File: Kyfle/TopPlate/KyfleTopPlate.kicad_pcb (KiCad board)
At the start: 2 copper layers, 164 x 146.3 mm, 44 parts, among them SW2 KEY_SWITCH, SW2 PRO MICRO

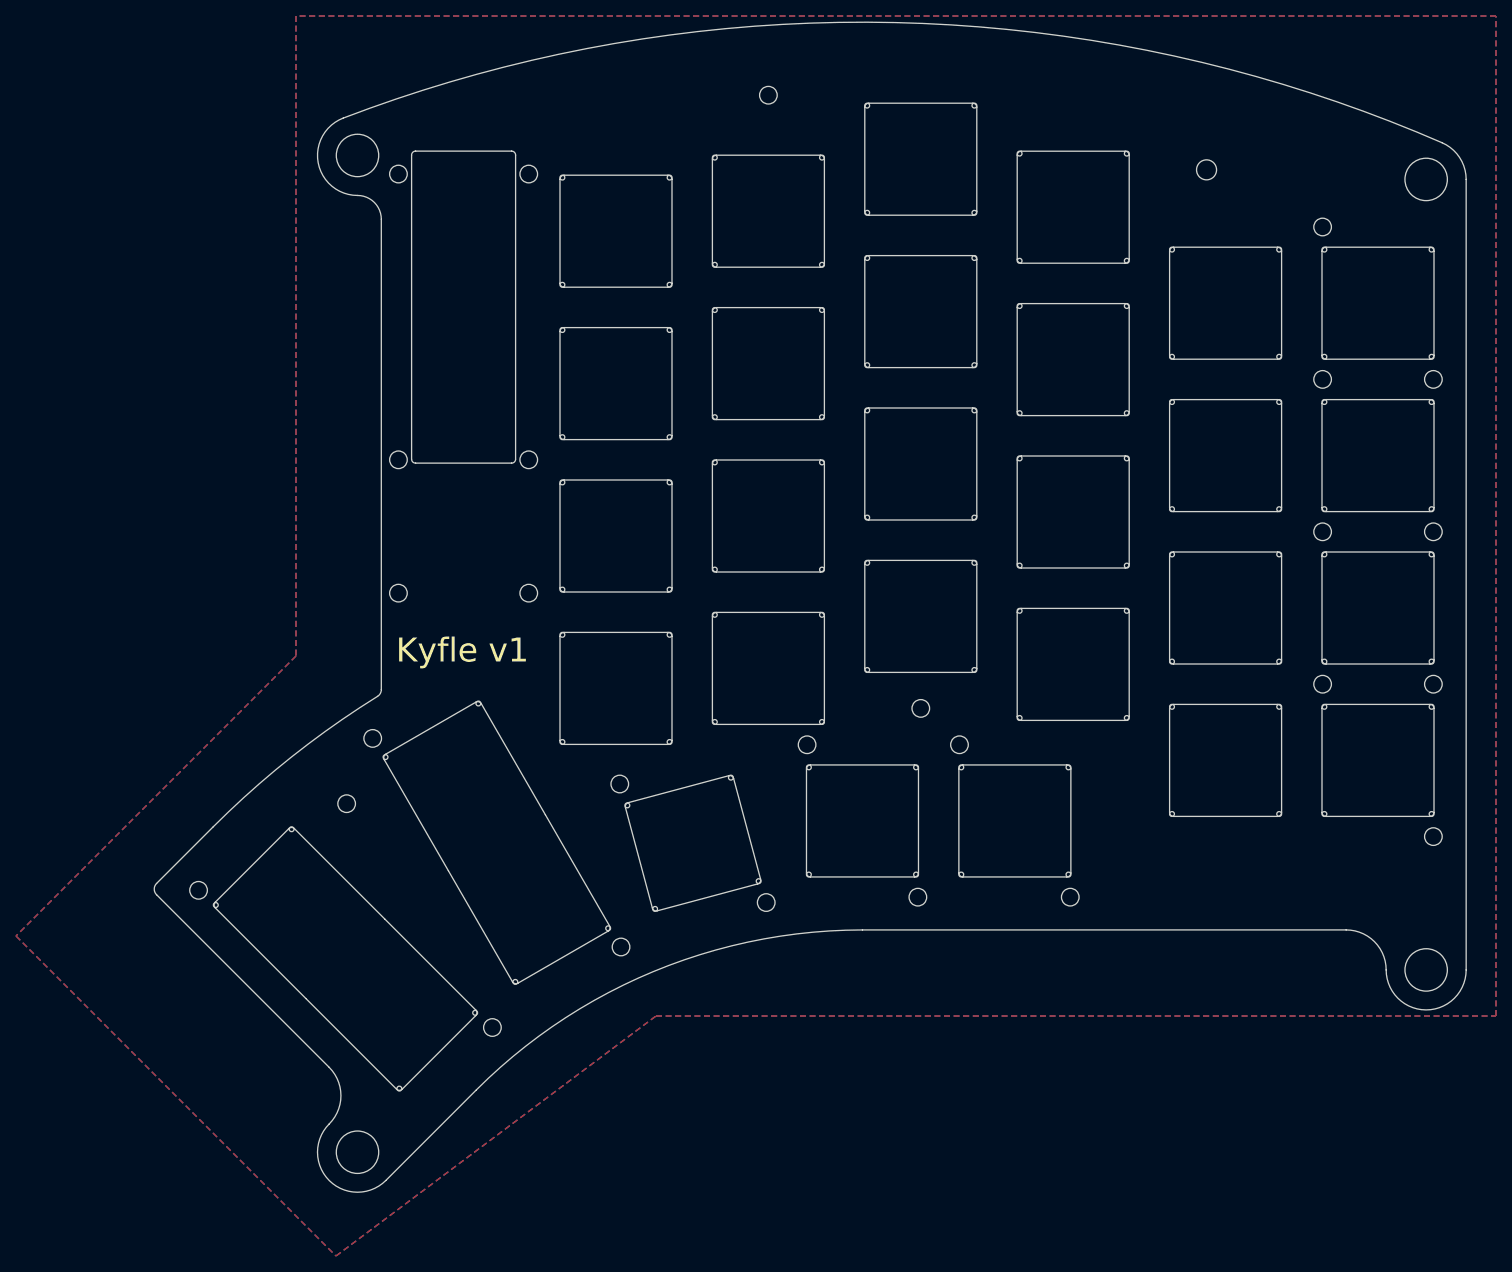
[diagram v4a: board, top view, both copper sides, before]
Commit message: Resized M2 slots and holes to 2mm instead of 2.2mm
After receiving M2 hardware, I noticed 2mm opening would provide a tighter and less wobbly fit than the typical M2 clearance of 2.2mm.

Also, finished the silkscreen of bottom plate, as well as M2 holes for encoders in top plate.
At this point, both top and bottom plate could be considered finished.
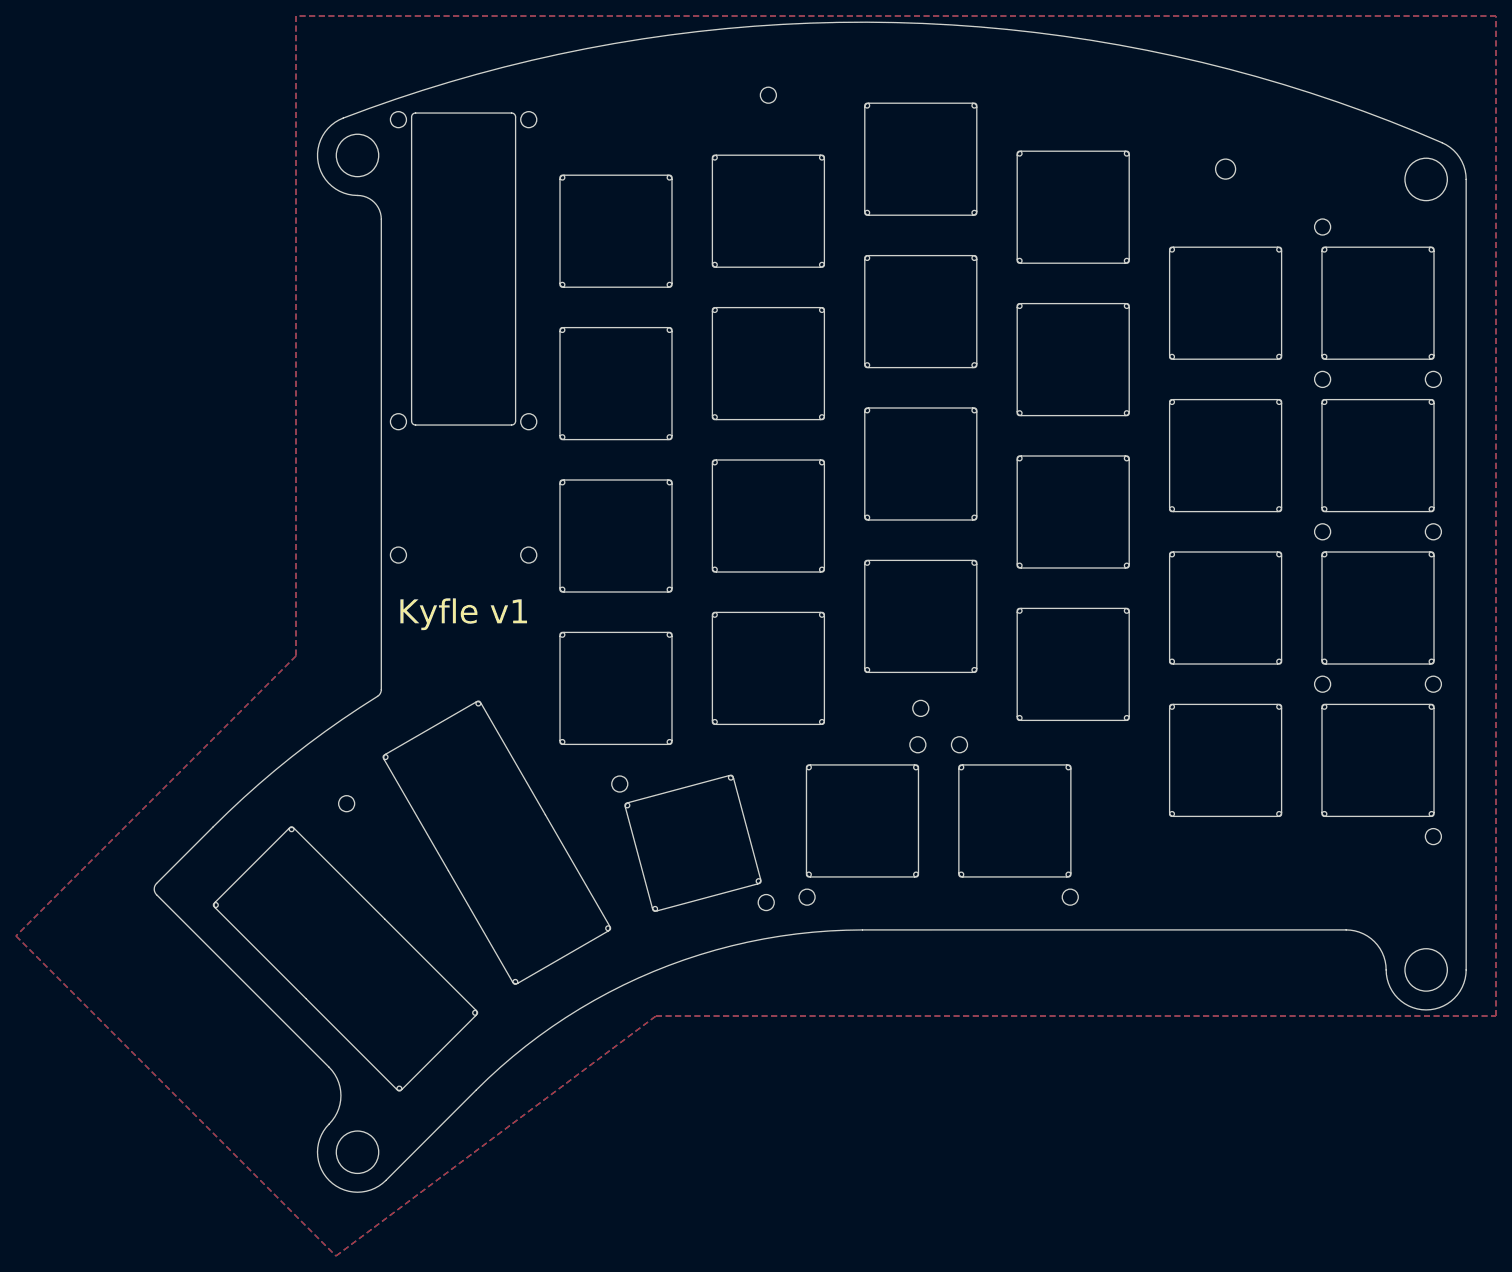
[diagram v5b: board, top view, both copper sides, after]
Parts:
- removed the REF** at (103.8, 37.3)
- removed the REF** at (120.0, 89.6)
- removed the REF** at (103.8, 89.6)
- removed the REF** at (103.8, 73.0)
- removed the REF** at (120.0, 73.0)
- removed the REF** at (120.0, 37.3)
- SW2: moved to B.Cu
- moved SW2 4.76 mm to (111.9, 58.7)
- moved SW2 2.38 mm to (207.2, 36.6)
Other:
- rule pad_to_mask_clearance: 0.2 -> 0

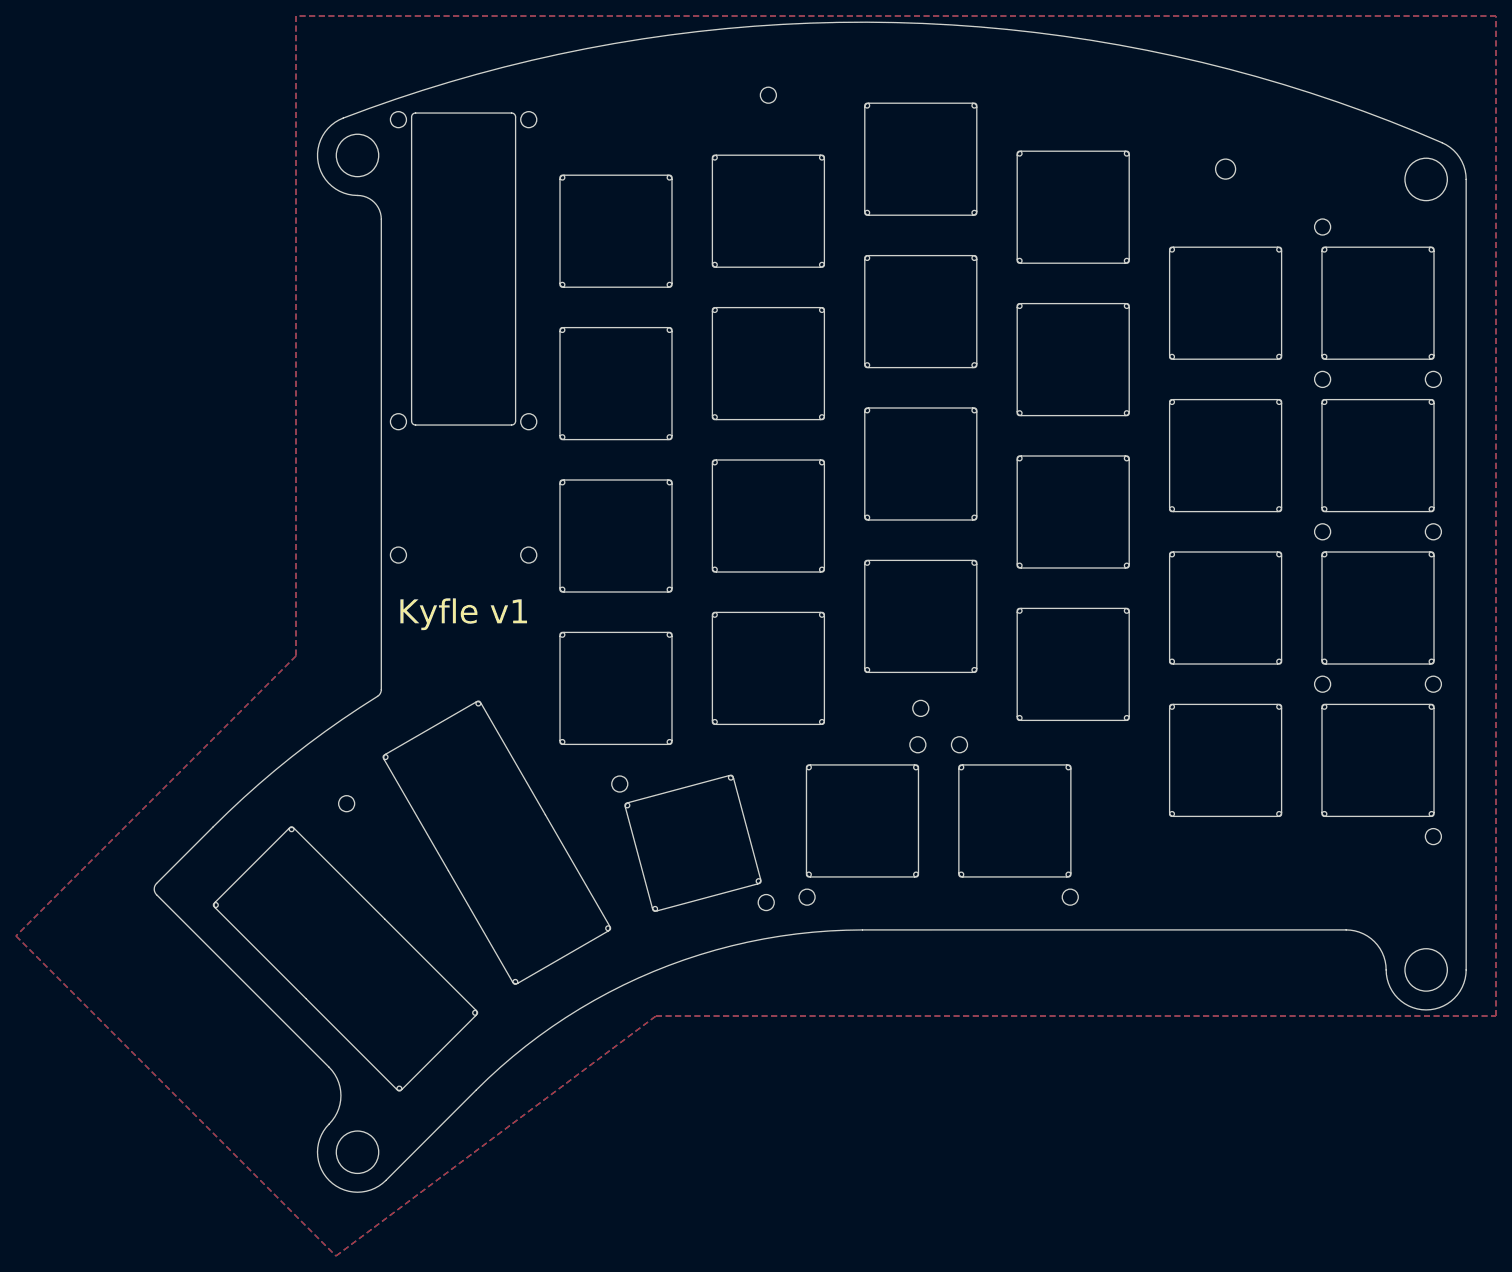
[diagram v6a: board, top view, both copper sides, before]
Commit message: It is never done. Adding plethora of plate variants.
- Variant of the default top plate with less routing involved
- Variant of a top plate allowing to slide the switches around
- Variant of that last top plate with less routing involved

Also moving few minor things here and there.
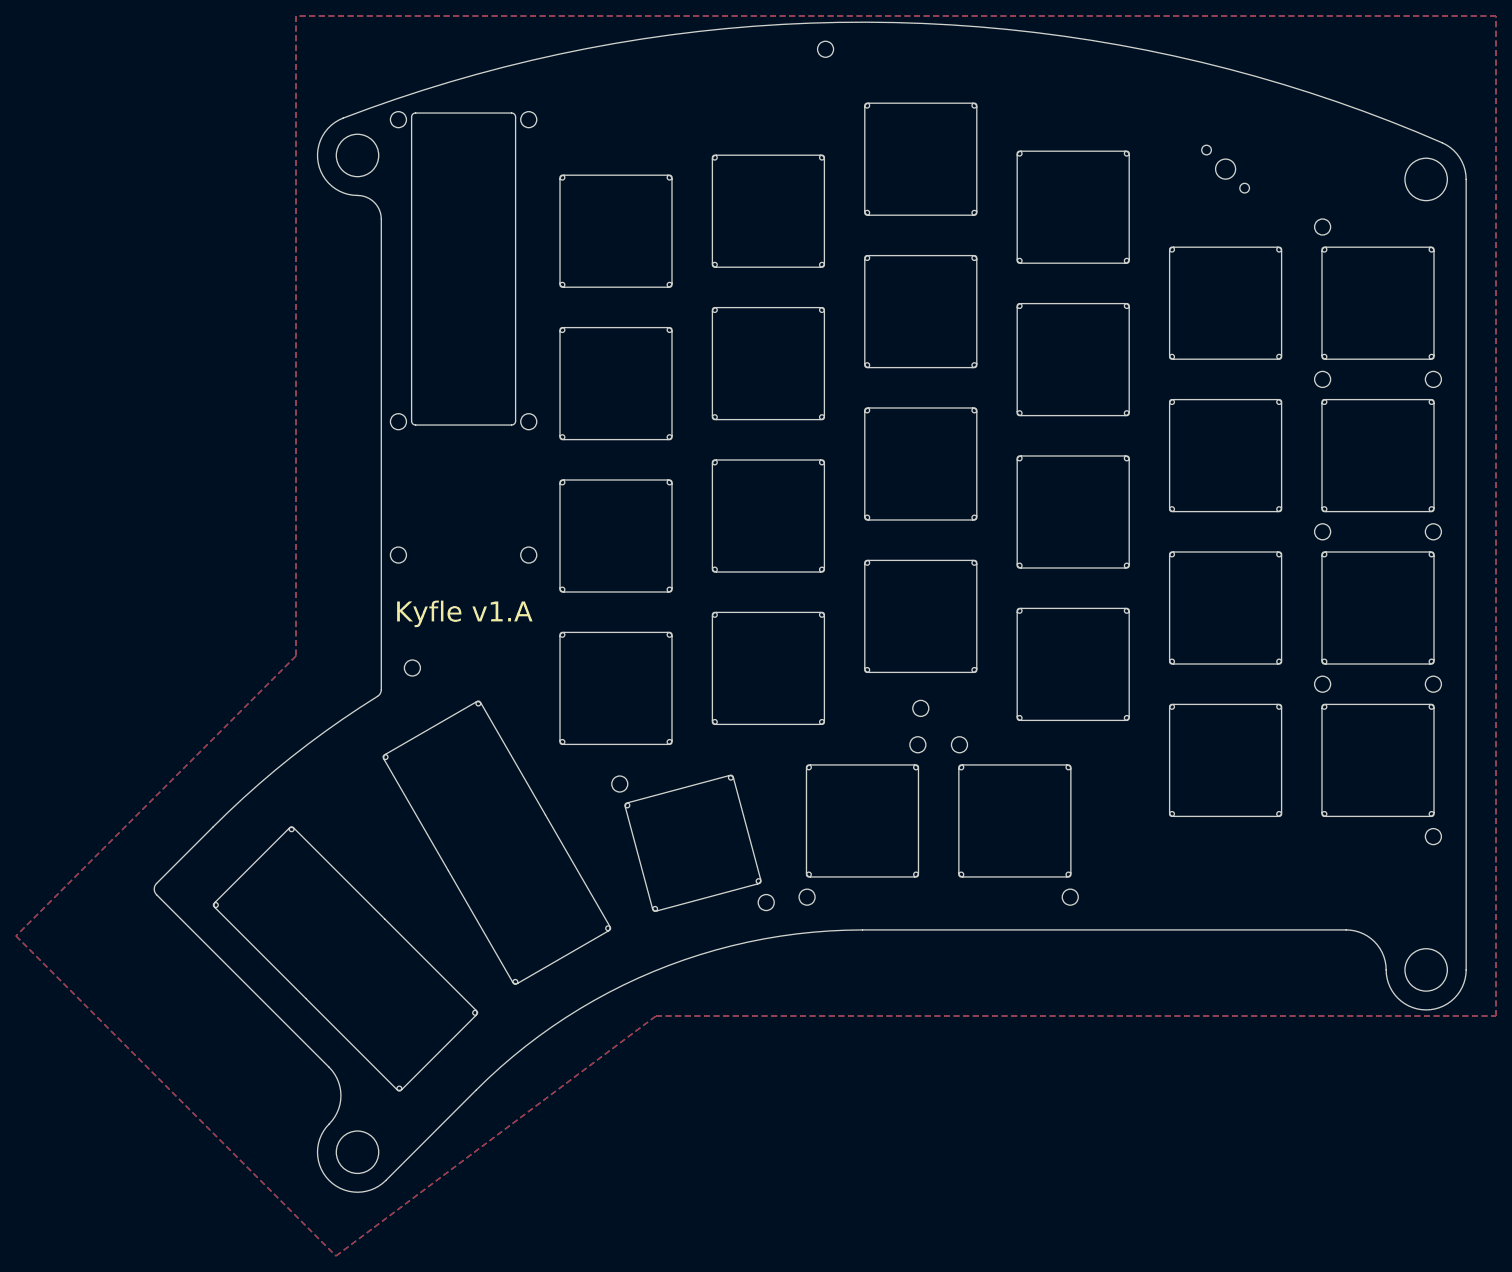
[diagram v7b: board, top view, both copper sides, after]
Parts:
- SW2: footprint Kyfle Footprints:SK6812_Bit -> Kyfle Footprints:SK6812_Bit_Bottom
- moved TH7 18.8 mm to (105.5, 99.0)
- moved TH3 9.16 mm to (157.1, 21.7)
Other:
- board text added: "Kyfle v1.A"
- board text removed: "Kyfle v1"
